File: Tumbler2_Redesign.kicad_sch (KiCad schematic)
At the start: 4 parts

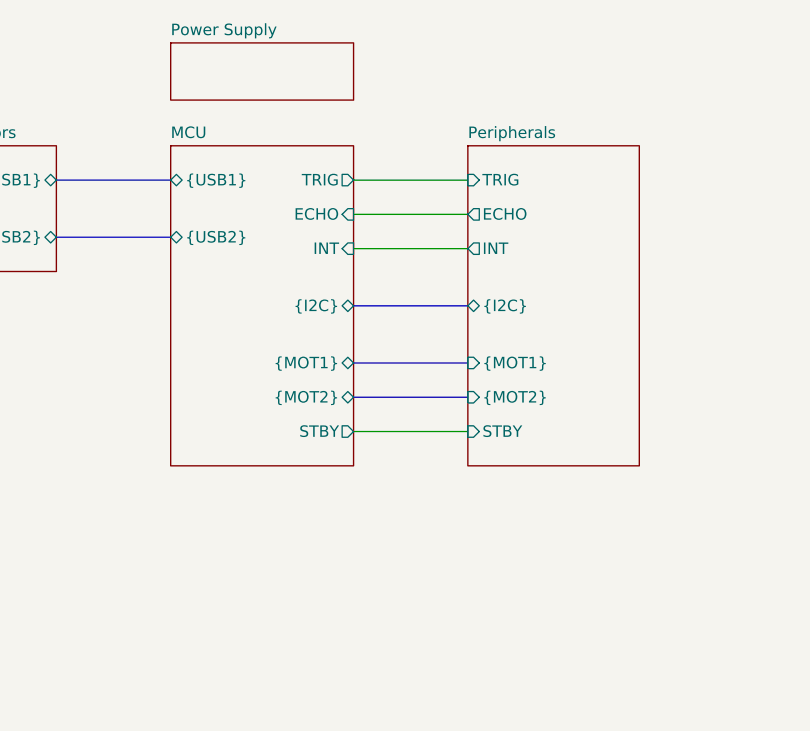
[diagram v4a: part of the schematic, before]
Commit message: Add missing rgb leds
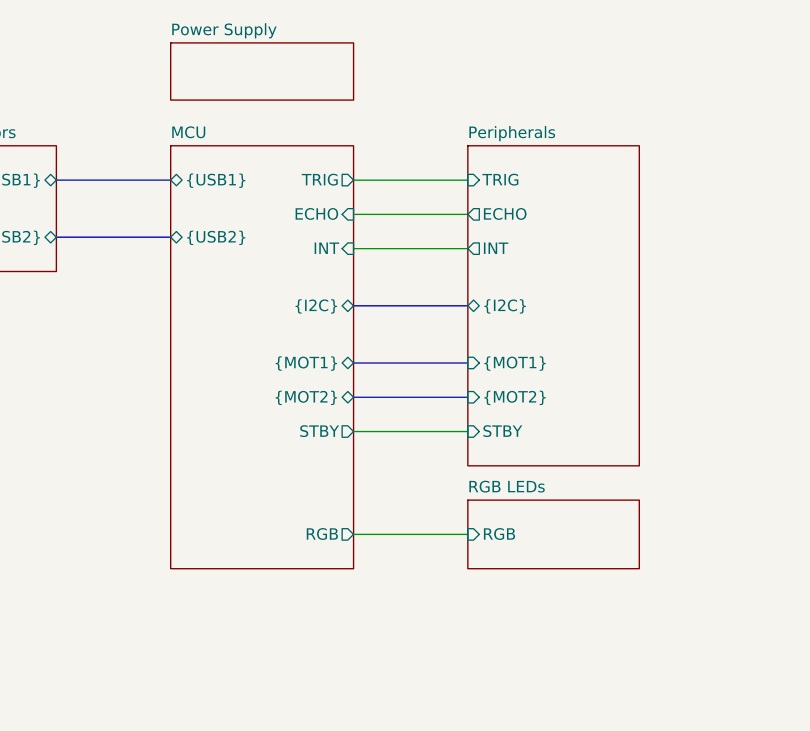
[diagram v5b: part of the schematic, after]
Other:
- added sheet RGB LEDs (rgb_leds.kicad_sch)
- sheet MCU ports: added RGB; removed none
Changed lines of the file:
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@@
+		)
+	)
+	(wire
+		(pts
+			(xy 153.67 127) (xy 166.37 127)
+		)
+		(stroke
+			(width 0)
+			(type default)
 		)
 	)
@@
 	(sheet
 		(at 133.35 83.82)
-		(size 20.32 35.56)
+		(size 20.32 46.99)
 		(exclude_from_sim no)
 		(in_bom yes)
@@
 		)
 		(property "Sheetfile" "mcu.kicad_sch"
-			(at 133.35 119.9646 0)
+			(at 133.35 131.3946 0)
 			(effects
 				(font
@@
 		(pin "{MOT2}" bidirectional
 			(at 153.67 111.76 0)
+			(effects
+				(font
+					(size 1.27 1.27)
+				)
+				(justify right)
+			)
+		)
+		(pin "RGB" output
+			(at 153.67 127 0)
 			(effects
 				(font
@@
 				)
 			)
+		)
+	)
+	(sheet
+		(at 166.37 123.19)
+		(size 19.05 7.62)
+		(exclude_from_sim no)
+		(in_bom yes)
+		(on_board yes)
+		(dnp no)
+		(fields_autoplaced yes)
+		(stroke
+			(width 0.1524)
+			(type solid)
+		)
+		(fill
+			(color 0 0 0 0.0000)
+		)
+		(property "Sheetname" "RGB LEDs"
+			(at 166.37 122.4784 0)
+			(effects
+				(font
+					(size 1.27 1.27)
+				)
+				(justify left bottom)
+			)
+		)
+		(property "Sheetfile" "rgb_leds.kicad_sch"
+			(at 166.37 131.3946 0)
+			(effects
+				(font
+					(size 1.27 1.27)
+				)
+				(justify left top)
+				(hide yes)
+			)
+		)
+		(pin "RGB" input
+			(at 166.37 127 180)
+			(effects
+				(font
+					(size 1.27 1.27)
+				)
+				(justify left)
+			)
+		)
+		(instances
+			(project "Tumbler2_Redesign"
+				(path "/f3fd8d79-9d35-4c04-811e-2697a2740958"
+					(page "6")
+				)
+			)

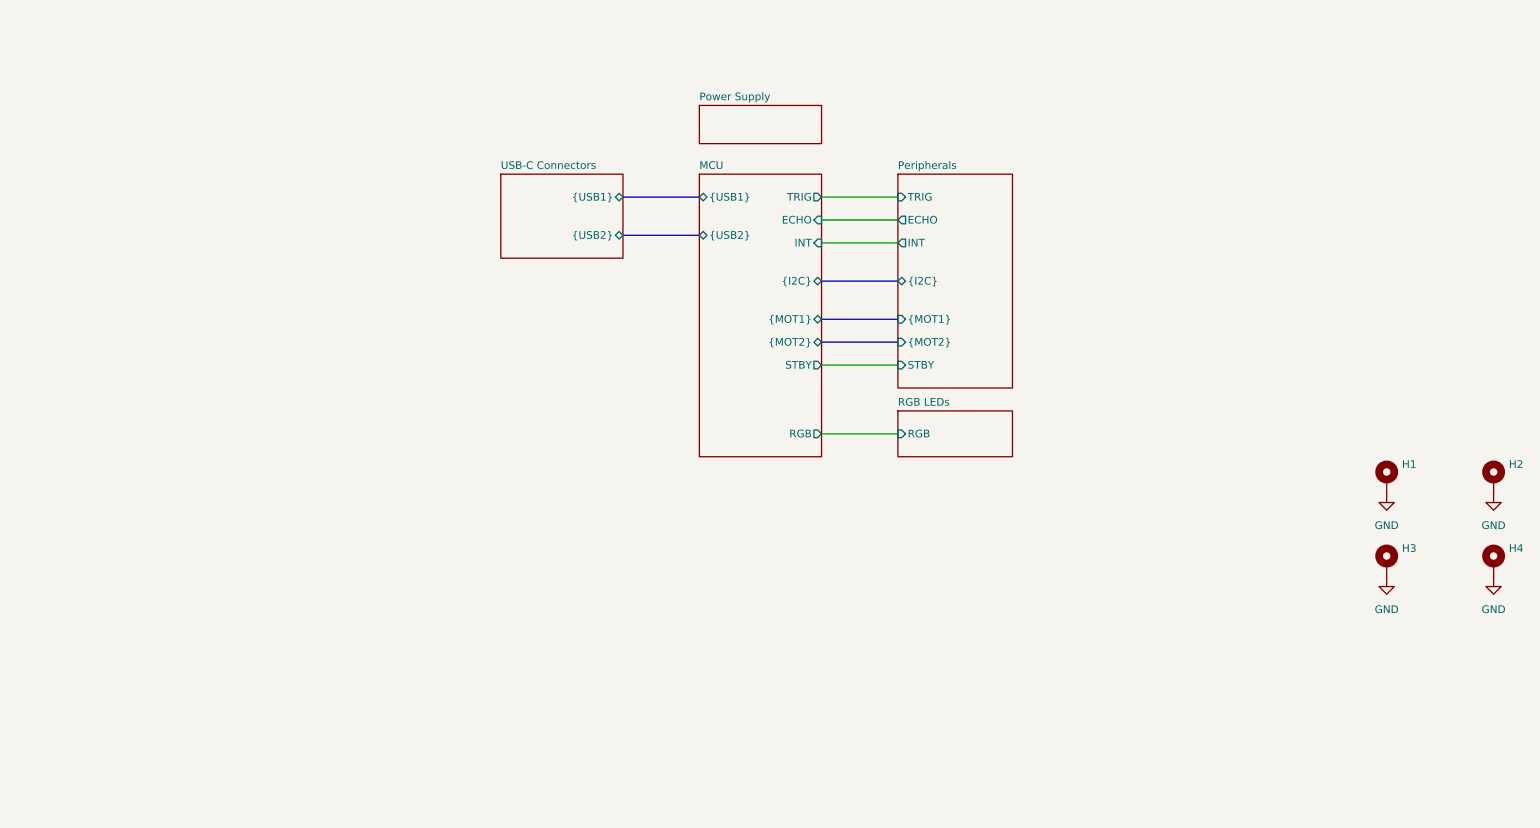
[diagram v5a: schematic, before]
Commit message: Add power rail block diagram
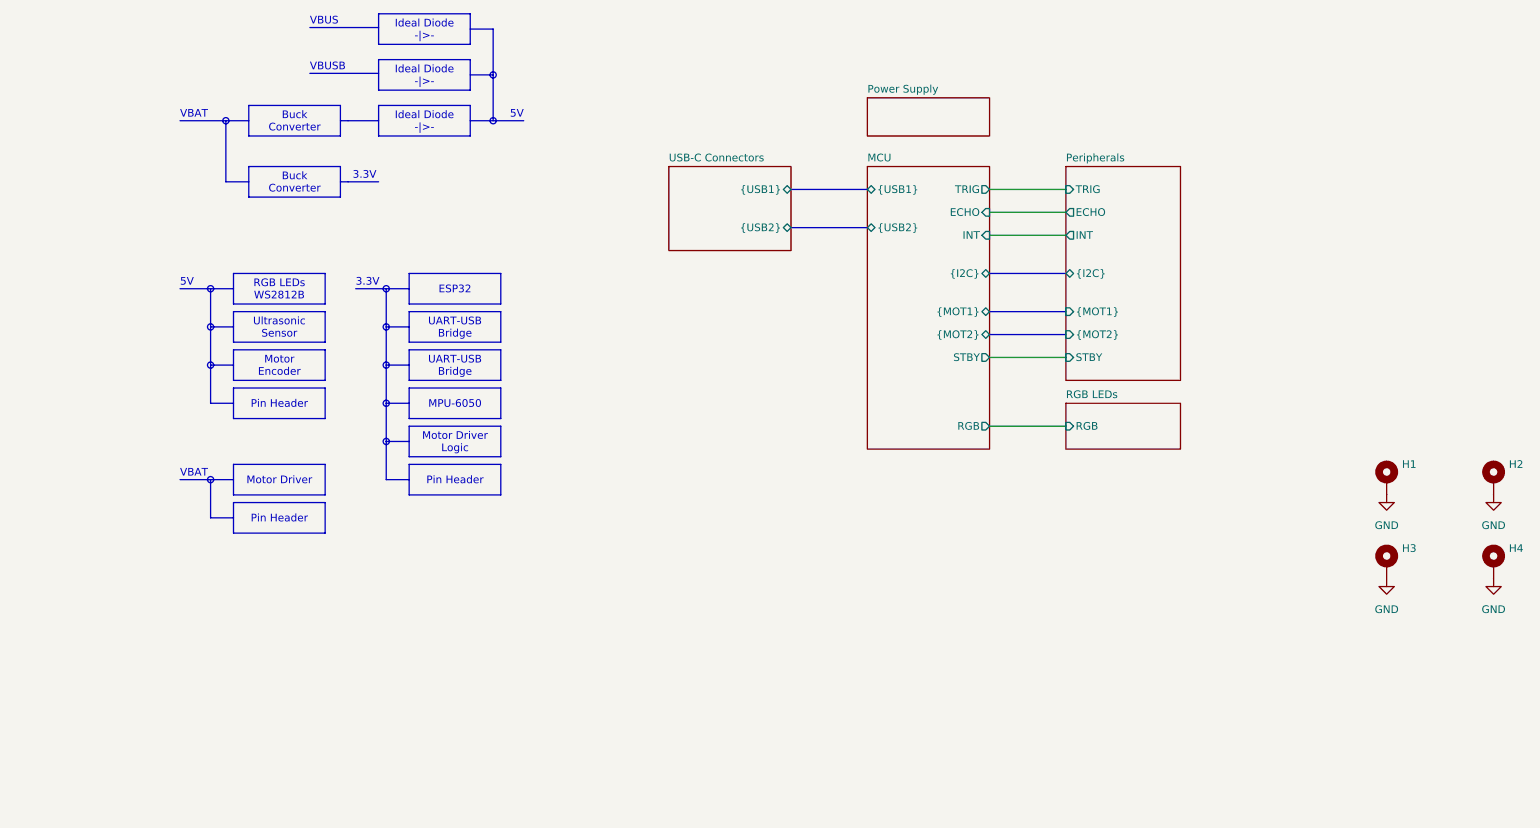
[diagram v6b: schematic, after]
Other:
- note added: "3.3V"
- note added: "5V"
- note added: "VBAT"
- note added: "VBUS"
- note added: "VBUSB"

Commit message: Replace with cheaper components
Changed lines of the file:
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@@
 		)
 	)
-	(text_box "Buck Converter"
+	(text_box "LDO"
 		(exclude_from_sim no)
 		(at 58.42 72.39 0)
@@
 			)
 		)
+		(property "SnapEDA_Link" ""
+			(at 247.65 148.59 0)
+			(effects
+				(font
+					(size 1.27 1.27)
+				)
+				(hide yes)
+			)
+		)
 		(pin "1"
 		)
@@
 			)
 		)
+		(property "SnapEDA_Link" ""
+			(at 265.43 148.59 0)
+			(effects
+				(font
+					(size 1.27 1.27)
+				)
+				(hide yes)
+			)
+		)
 		(pin "1"
 		)
@@
 			)
 		)
+		(property "SnapEDA_Link" ""
+			(at 265.43 134.62 0)
+			(effects
+				(font
+					(size 1.27 1.27)
+				)
+				(hide yes)
+			)
+		)
 		(pin "1"
 		)
@@
 			(at 247.65 134.62 0)
 			(effects
+				(font
+					(size 1.27 1.27)
+				)
+				(hide yes)
+			)
+		)
+		(property "SnapEDA_Link" ""
+			(at 247.65 134.62 0)
+			(effects
